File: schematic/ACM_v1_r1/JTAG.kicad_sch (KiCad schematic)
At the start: 33 parts, among them J4 USB-Debug, U1 FT2232HL, Y1 12MHz/10pF

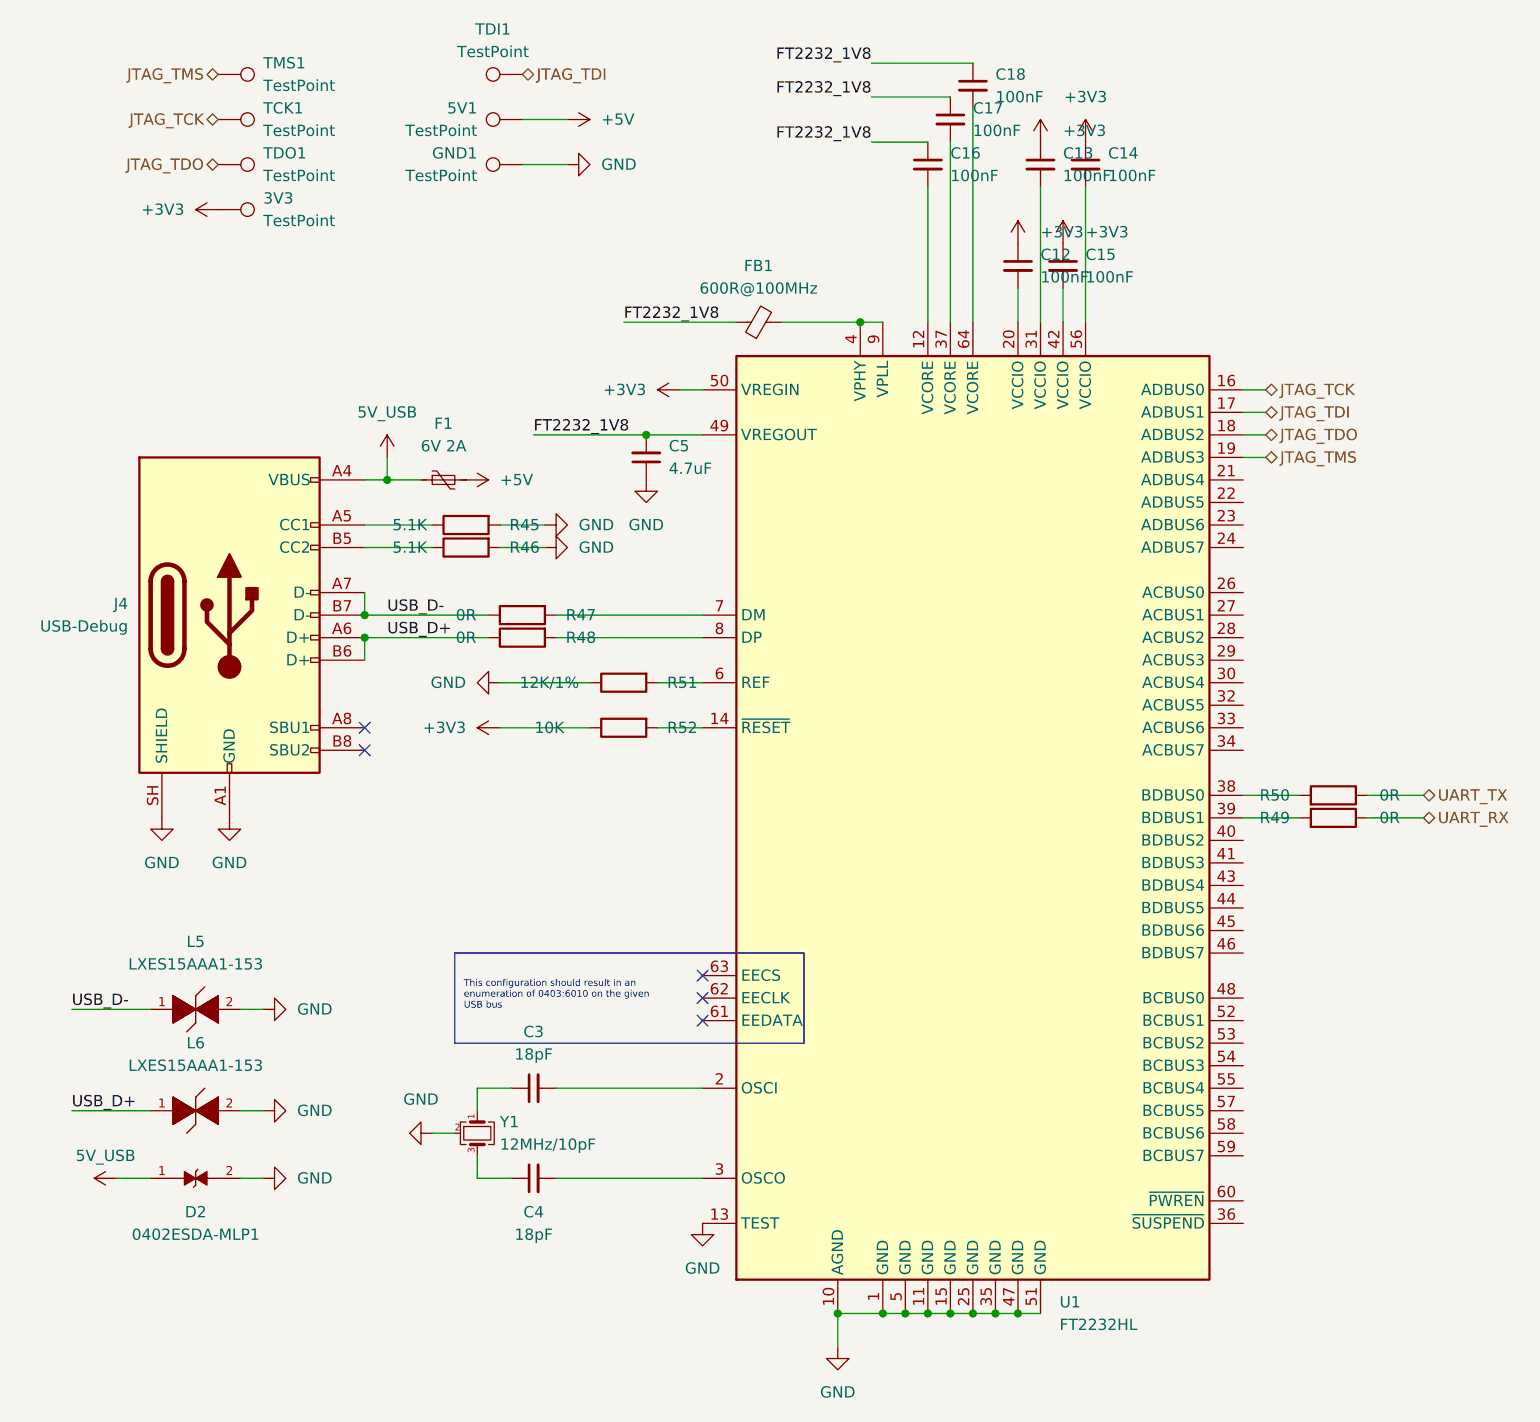
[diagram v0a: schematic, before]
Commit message: ACM module board routed
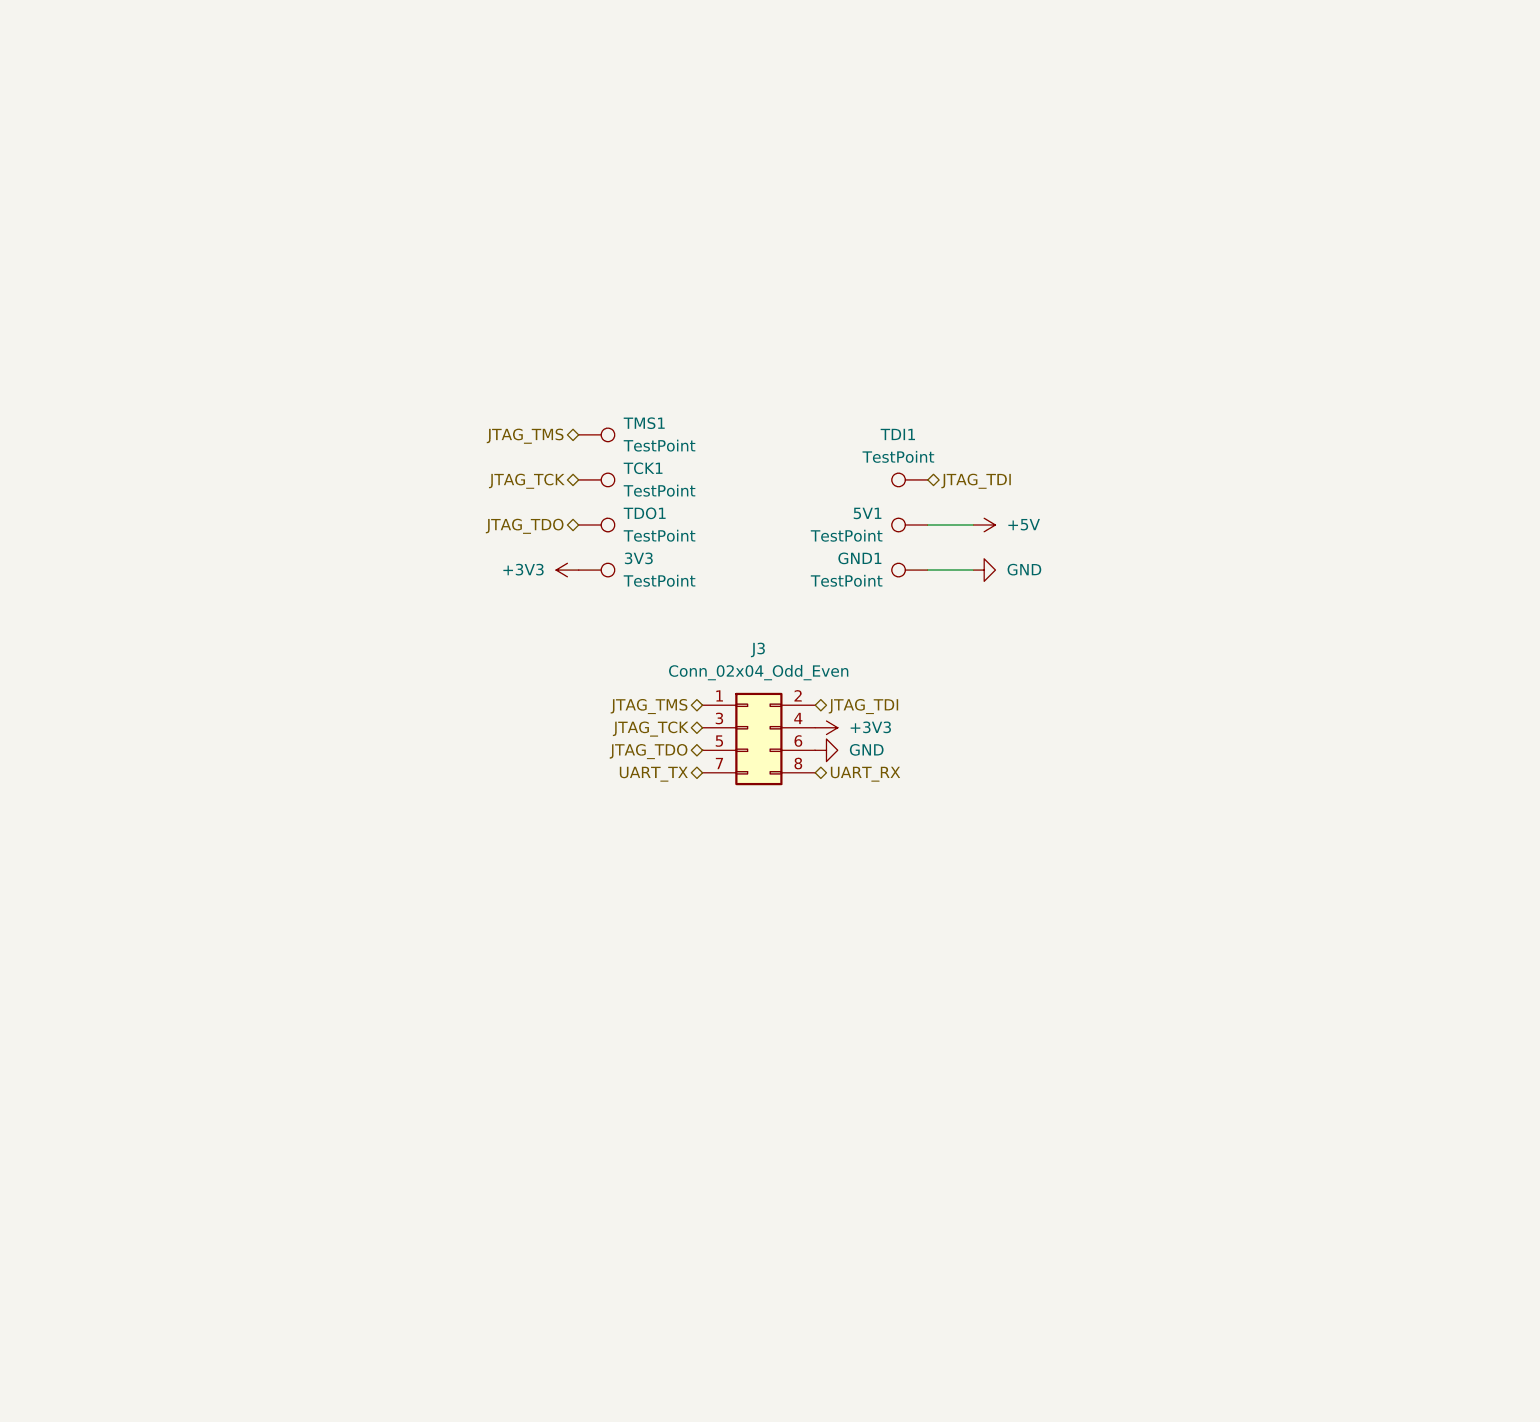
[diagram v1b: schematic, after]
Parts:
- removed C12, C13, C14, C15, C16, C17, C18: 100nF, Capacitor_SMD:C_0805_2012Metric, symbol Device:C_Small
- removed C3, C4: 18pF, Capacitor_SMD:C_0805_2012Metric, symbol Device:C_Small
- removed C5: 4.7uF, Capacitor_SMD:CP_Elec_4x3, symbol Device:C_Small
- removed D2: 0402ESDA-MLP1, my_footprints:ESD_0402ESDA-MLP1, symbol 0402ESDA-MLP1:0402ESDA-MLP1
- removed F1: 6V 2A, Fuse:Fuse_0603_1608Metric, symbol Device:Polyfuse_Small
- removed FB1: 600R@100MHz, Inductor_SMD:L_0603_1608Metric, symbol Device:FerriteBead_Small
- removed J4: USB-Debug, Connector_USB:USB_C_Receptacle_GCT_USB4105-xx-A_16P_TopMnt_Horizontal, symbol Connector:USB_C_Receptacle_USB2.0_16P
- removed L5, L6: LXES15AAA1-153, my_footprints:INDC1005X45, symbol LXES15AAA1-153:LXES15AAA1-153
- removed R45, R46: 5.1K, Resistor_SMD:R_0201_0603Metric, symbol Device:R
- removed R47, R48, R49, R50: 0R, Resistor_SMD:R_0201_0603Metric, symbol Device:R
- removed R51: 12K/1%, Resistor_SMD:R_0201_0603Metric, symbol Device:R
- removed R52: 10K, Resistor_SMD:R_0201_0603Metric, symbol Device:R
- removed U1: FT2232HL, Package_QFP:LQFP-64_10x10mm_P0.5mm, symbol Interface_USB:FT2232HL
- removed Y1: 12MHz/10pF, Crystal:Crystal_SMD_2016-4Pin_2.0x1.6mm, symbol Device:Crystal_GND24_Small
- added J3: Conn_02x04_Odd_Even, Connector_PinHeader_2.54mm:PinHeader_2x04_P2.54mm_Vertical_SMD, symbol Connector_Generic:Conn_02x04_Odd_Even
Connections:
- net +3V3: now also J3.4 (Pin_4)
- net GND: now also J3.6 (Pin_6)
- net JTAG_TCK: now also J3.3 (Pin_3)
- net JTAG_TDI: now also J3.2 (Pin_2)
- net JTAG_TDO: now also J3.5 (Pin_5)
- net JTAG_TMS: now also J3.1 (Pin_1)
- net UART_RX: now also J3.8 (Pin_8)
- net UART_TX: now also J3.7 (Pin_7)
- no-connect marks 5 -> 0
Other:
- note removed: "This configuration should result in an enumeration of 0403:6010 on the given USB bus"
- moved on the sheet: 3V3, 5V1, GND1, TCK1, TDI1, TDO1, TMS1
